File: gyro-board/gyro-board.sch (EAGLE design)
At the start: 27 parts, among them U1 LY3200, U2 LY3200, U3 LY3200

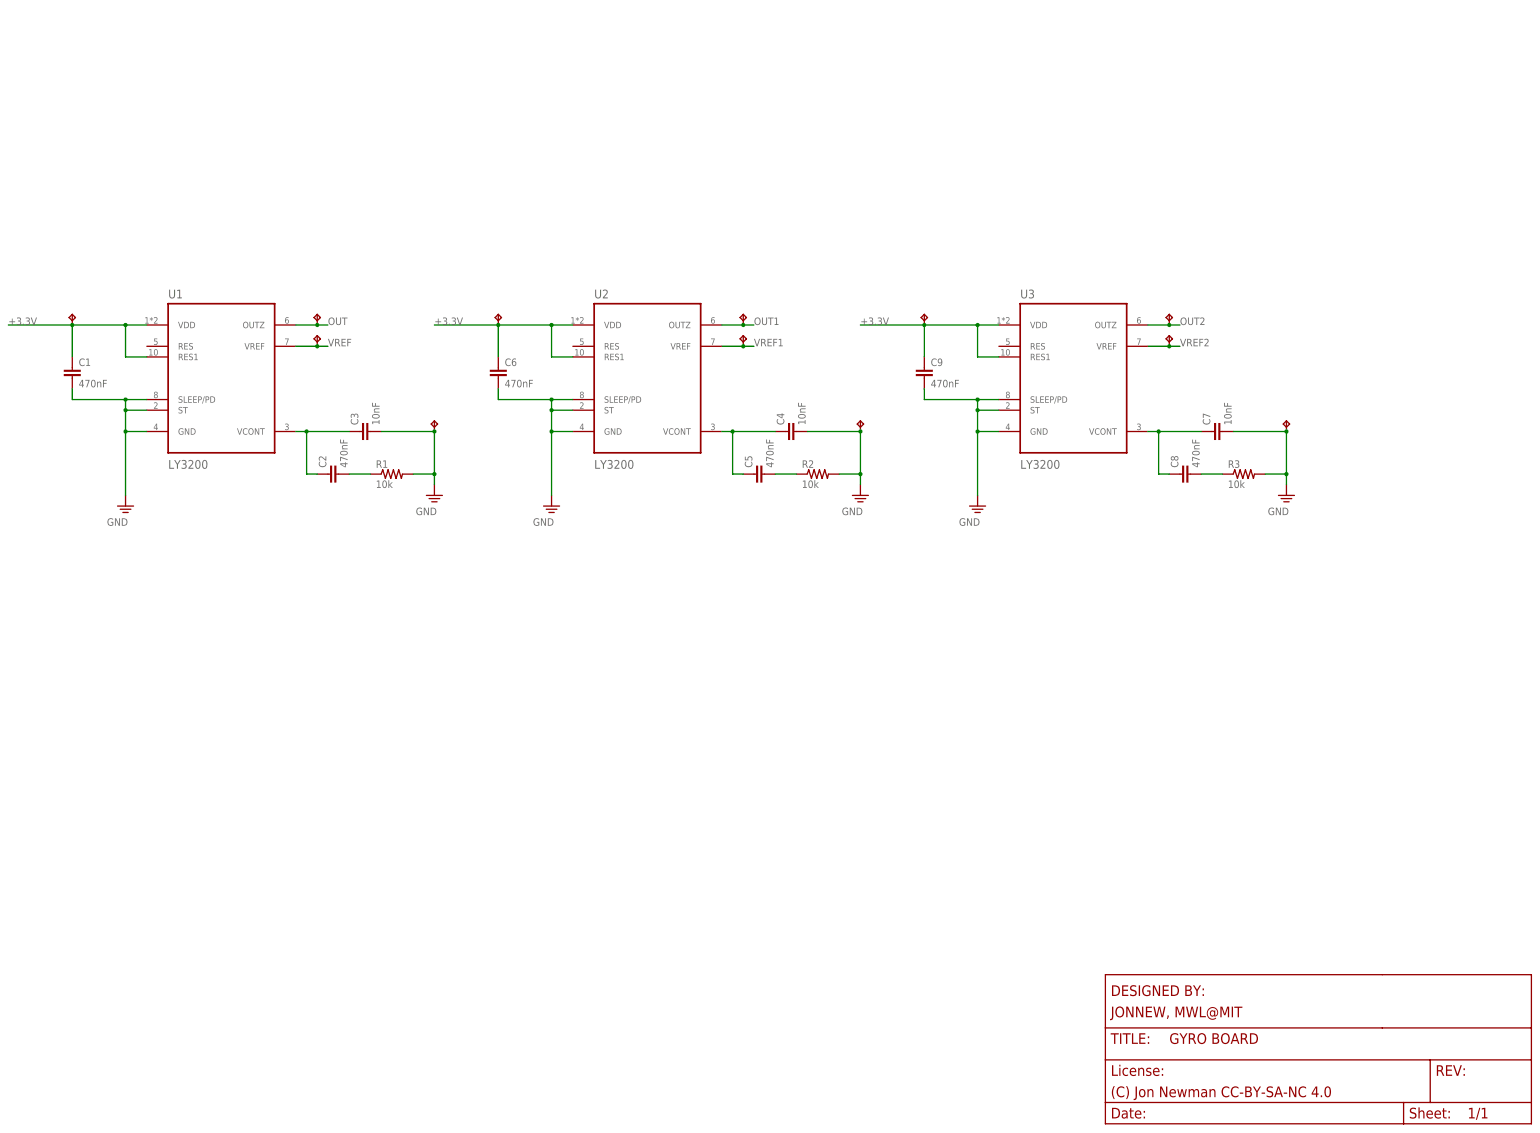
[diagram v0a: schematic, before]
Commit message: Sent three boards out for printing
- 24 circuit commutator adapter
- 12 circuit commutator adapter
- Gyro board (really just for testing before integration with SPI
  interface board)
- Need to update BOM sheet to include these guys
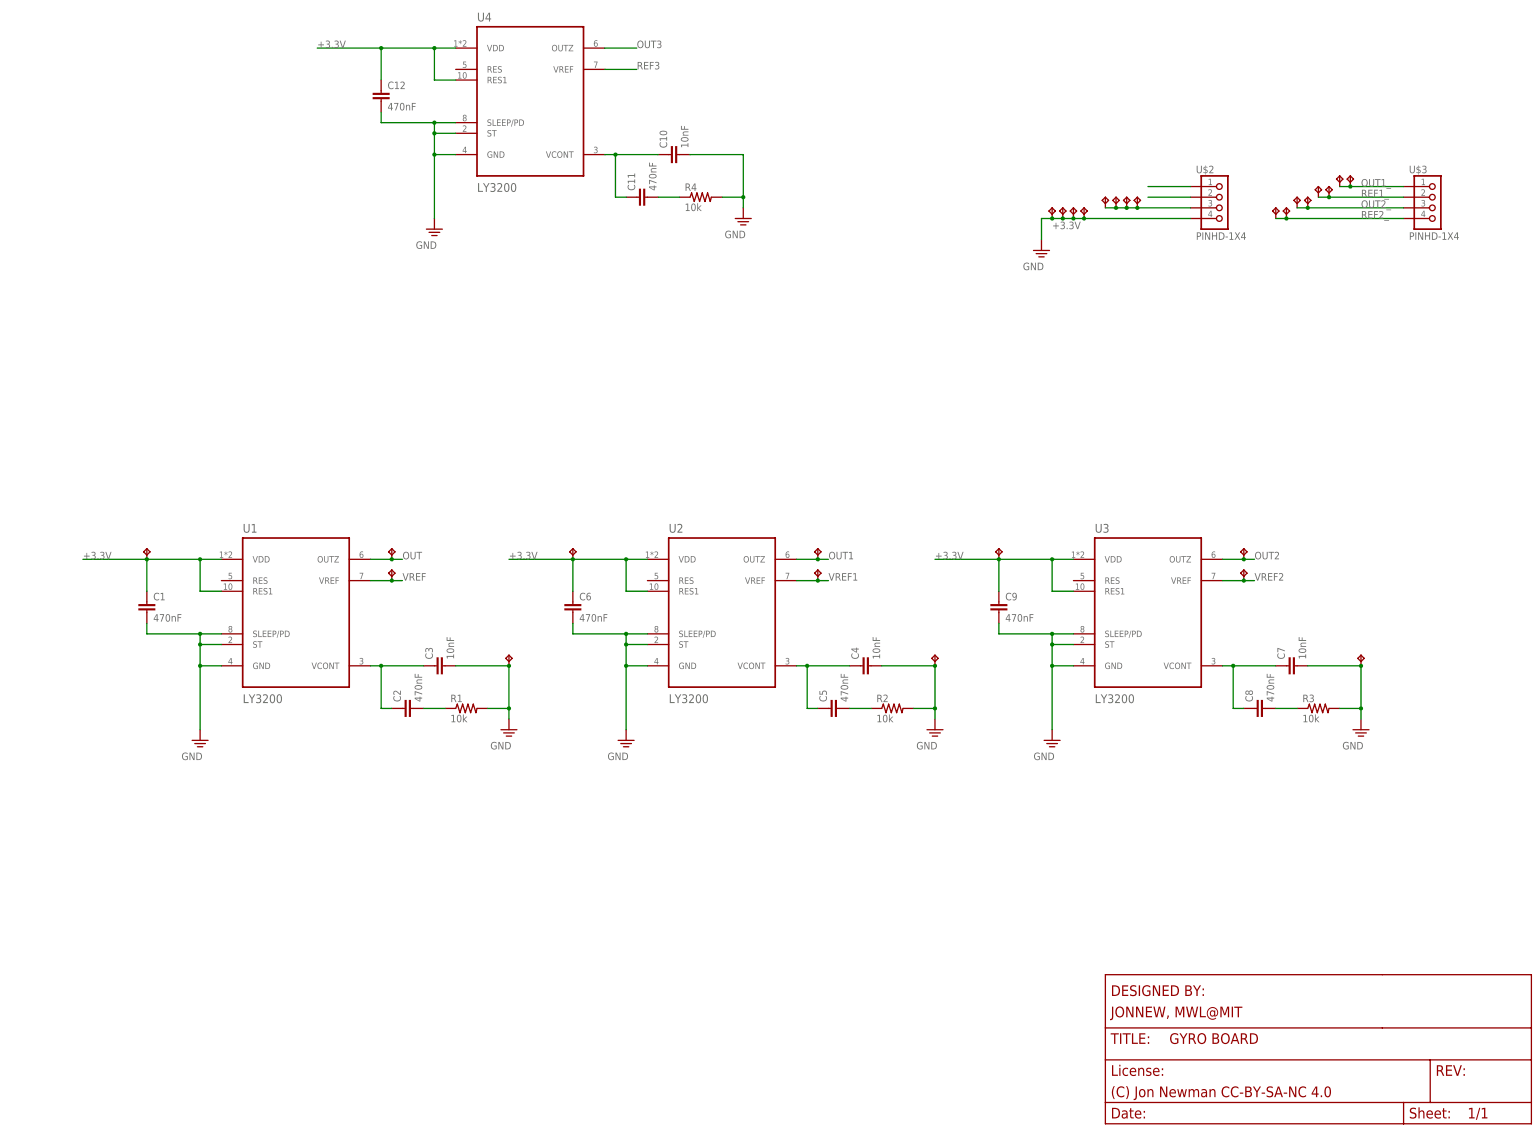
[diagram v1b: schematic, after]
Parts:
- added C10: 10nF, jonnew:C_0201
- added C11, C12: 470nF, jonnew:C_0201
- added R4: 10k, jonnew:R_0201
- added TP13, TP14, TP15, TP16, TP17, TP18, TP19, TP20, TP21, TP22, TP23, TP24, TP25, TP26, TP27, TP28: (no value), jonnew:TPTP08SQ
- added U$2, U$3: PINHD-1X4, jonnew:PINHD-1X4
- added U4: LY3200, jonnew:LY3200ALH_LGA-10-COMPACT
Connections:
- new net N$7: C10.1, C11.1, U4.VCONT
- new net N$8: C11.2, R4.1
- new net OUT1_: TP20.TP, TP21.TP, U$3.1
- new net OUT2_: TP16.TP, TP17.TP, U$3.3
- new net OUT3: U$2.1, U4.OUTZ
- new net REF1_: TP18.TP, TP19.TP, U$3.2
- new net REF2_: TP14.TP, TP15.TP, U$3.4
- new net REF3: U$2.2, U4.VREF
- net +3.3V: now also C12.1, TP25.TP, TP26.TP, TP27.TP, TP28.TP, U$2.3, U4.RES1, U4.VDD
- net GND: now also C10.2, C12.2, R4.2, TP13.TP, TP22.TP, TP23.TP, TP24.TP, U$2.4, U4.GND, U4.SLEEP/PD, U4.ST
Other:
- moved on the sheet: C1, C2, C3, C4, C5, C6, C7, C8, C9, R1, R2, R3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
